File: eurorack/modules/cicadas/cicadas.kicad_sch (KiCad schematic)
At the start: 54 parts, among them J1 Conn_02x05_Odd_Even, J10 AudioJack2_SwitchT, J11 AudioJack2_SwitchT, J2 AVR-ISP-6, J3 AudioJack2_SwitchT, J4 AudioJack2_SwitchT, J5 AudioJack2_SwitchT, J6 AudioJack2_SwitchT, J7 AudioJack2_SwitchT, J8 AudioJack2_SwitchT, J9 AudioJack2_SwitchT, U1 L78L33_SOT89, U2 ATmega328P-A, U3 MCP4822, U4 MCP4822

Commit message: initial work on cicadas v3
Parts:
- removed C2: 100n, Capacitor_SMD:C_0805_2012Metric_Pad1.18x1.45mm_HandSolder, symbol Device:C
- removed D4: LED, LED_SMD:LED_0805_2012Metric_Pad1.15x1.40mm_HandSolder, symbol Device:LED
- removed J2: AVR-ISP-6, Connector_PinHeader_2.54mm:PinHeader_2x03_P2.54mm_Vertical_SMD, symbol Connector:AVR-ISP-6
- removed R2: R, Resistor_SMD:R_0805_2012Metric_Pad1.20x1.40mm_HandSolder, symbol Device:R
- removed TP1: 3.3V, TestPoint:TestPoint_Pad_D1.5mm, symbol Connector:TestPoint
- removed TP10: B, TestPoint:TestPoint_Pad_D1.5mm, symbol Connector:TestPoint
- removed TP11: A4, TestPoint:TestPoint_Pad_D1.5mm, symbol Connector:TestPoint
- removed TP12: A3, TestPoint:TestPoint_Pad_D1.5mm, symbol Connector:TestPoint
- removed TP13: GND, TestPoint:TestPoint_Pad_D1.5mm, symbol Connector:TestPoint
- removed TP2: D4, TestPoint:TestPoint_Pad_D1.5mm, symbol Connector:TestPoint
- removed TP3: D3, TestPoint:TestPoint_Pad_D1.5mm, symbol Connector:TestPoint
- removed TP4: D2, TestPoint:TestPoint_Pad_D1.5mm, symbol Connector:TestPoint
- removed TP5: A2, TestPoint:TestPoint_Pad_D1.5mm, symbol Connector:TestPoint
- removed TP6: D1, TestPoint:TestPoint_Pad_D1.5mm, symbol Connector:TestPoint
- removed TP7: A1, TestPoint:TestPoint_Pad_D1.5mm, symbol Connector:TestPoint
- removed TP8: R, TestPoint:TestPoint_Pad_D1.5mm, symbol Connector:TestPoint
- removed TP9: G, TestPoint:TestPoint_Pad_D1.5mm, symbol Connector:TestPoint
- removed U1: L78L33_SOT89, Package_TO_SOT_SMD:SOT-89-3, symbol Regulator_Linear:L78L33_SOT89
- removed U2: ATmega328P-A, Package_QFP:TQFP-32_7x7mm_P0.8mm, symbol MCU_Microchip_ATmega:ATmega328P-A
- added D10, D11, D4, D5, D6, D7, D8, D9: SK6812MINI, Pale Slim Ghost:SK6812MINI-E, symbol kbd:YS-SK6812MINI-E
- added G1, G2: (no value), symbol Pale Slim Ghost:Artwork
- added H1, H10, H11, H12, H2, H3, H4, H5, H6, H7, H8, H9: (no value), symbol Mechanical:MountingHole
- added U1: ProMicro, promicro:ProMicro-NoSilk, symbol promicro:ProMicro
- J10, J11, J3, J4, J5, J6, J7, J8, J9: footprint AudioJacks:Jack_3.5mm_QingPu_WQP-PJ398SM_Vertical -> (none)
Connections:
- net +12V: now also U1.24 (RAW)
- net +3V3: now also D10.1 (VDD), D11.1 (VDD), D4.1 (VDD), D5.1 (VDD), D6.1 (VDD), D7.1 (VDD), D8.1 (VDD), D9.1 (VDD), U1.21 (VCC)
- net CIPO: now also U1.15 (B3)
- net COPI: now also U1.14 (B2)
- net CS1: now also U1.12 (B5)
- net CS2: now also U1.11 (B4)
- net D1: now also U1.17 (F7)
- net D2: now also U1.18 (F6)
- net D3: now also U1.19 (F5)
- net D4: now also U1.20 (F4)
- net GND: now also D10.3 (VSS), D11.3 (VSS), D4.3 (VSS), D5.3 (VSS), D6.3 (VSS), D7.3 (VSS), D8.3 (VSS), D9.3 (VSS), U1.23 (GND), U1.3 (GND), U1.4 (GND)
- net LED B: now also U1.9 (D7)
- net LED G: now also U1.8 (C6)
- net LED R: now also U1.6 (SCL)
- net SCK: now also U1.16 (B1)
- net clock in: now also U1.5 (SDA)
- net encoder A: now also U1.1 (TX)
- net encoder B: now also U1.2 (RX)
- net switch: now also U1.7 (D4)
- new net: D10.4 (DIN), D9.2 (DOUT)
- new net: D8.2 (DOUT), D9.4 (DIN)
- new net: D7.2 (DOUT), D8.4 (DIN)
- new net: D6.2 (DOUT), D7.4 (DIN)
- new net: D10.2 (DOUT), D11.4 (DIN)
- new net: D4.2 (DOUT), D5.4 (DIN)
- new net: D5.2 (DOUT), D6.4 (DIN)
- new net LED: D4.4 (DIN), U1.13 (B6)
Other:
- moved on the sheet: C1, C4, D1, D2, J1

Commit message: cicadas footprint associations
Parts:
- G1: value (none) -> Artwork; footprint (none) -> Pale Slim Ghost:logo
- G2: value (none) -> Artwork
- H1, H12: value (none) -> MountingHole; footprint (none) -> Pale Slim Ghost:eurorack panel mounting slot
- H10, H11, H2, H4, H5, H6, H7, H8, H9: value (none) -> MountingHole; footprint (none) -> Pale Slim Ghost:hole 6mm (jack panel)
- H3: value (none) -> MountingHole; footprint (none) -> Pale Slim Ghost:hole 9mm (encoder panel)
- J10, J11, J3, J4, J5, J6, J7, J8, J9: footprint (none) -> Pale Slim Ghost:Jack_3.5mm_QingPu_WQP-PJ398SM_Vertical

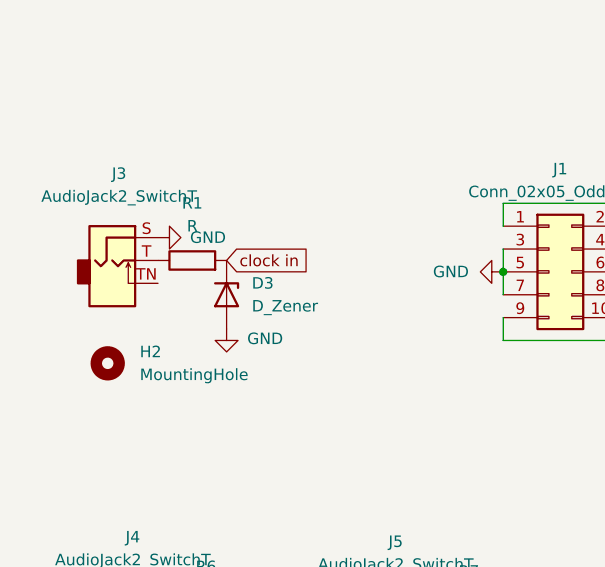
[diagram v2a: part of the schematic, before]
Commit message: cicadas: normal clock input to 3v3 and fix missing ground connections
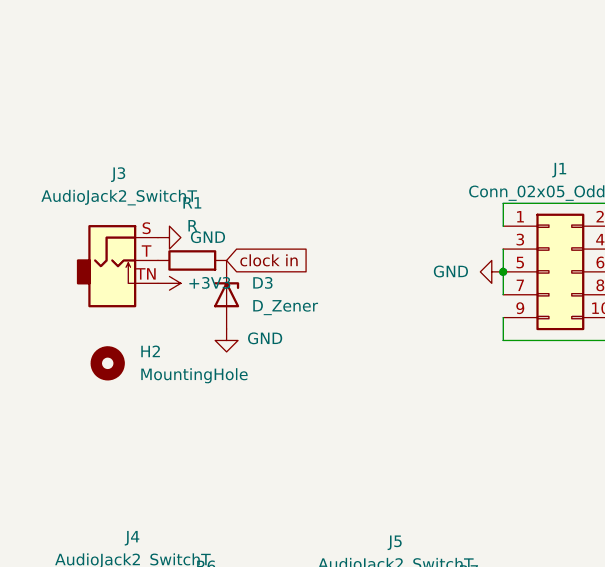
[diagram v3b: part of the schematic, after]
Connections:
- net +3V3: now also J3.TN
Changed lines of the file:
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@@
     (pin "9")
+  )
+  (symbol (lib_id "power:+3V3") (at 35.306 53.34 270) (unit 1)
+    (in_bom yes) (on_board yes) (fields_autoplaced)
+    (property "Reference" "#PWR?" (id 0) (at 31.496 53.34 0)
+      (effects (font (size 1.27 1.27)) hide)
+    )
+    (property "Value" "+3V3" (id 1) (at 38.608 53.3399 90)
+      (effects (font (size 1.27 1.27)) (justify left))
+    )
+    (property "Footprint" "" (id 2) (at 35.306 53.34 0)
+      (effects (font (size 1.27 1.27)) hide)
+    )
+    (property "Datasheet" "" (id 3) (at 35.306 53.34 0)
+      (effects (font (size 1.27 1.27)) hide)
+    )
+    (pin "1")
   )
   (symbol (lib_id "power:GND") (at 73.66 52.07 270) (unit 1)
@@
       (reference "#PWR0106") (unit 1) (value "GND") (footprint "")
     )
+    (path "/89197813-1f34-412e-b0f2-543175929a5d"
+      (reference "#PWR?") (unit 1) (value "+3V3") (footprint "")
+    )
     (path "/f39590a6-380e-454f-af5a-71361c77cf95"

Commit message: wip cicadas redesign
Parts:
- removed C1: 10u, Capacitor_SMD:CP_Elec_5x4.5, symbol Device:C_Polarized
- removed C4: 100n, Capacitor_SMD:C_0805_2012Metric_Pad1.18x1.45mm_HandSolder, symbol Device:C
- removed D1, D2: D, Diode_SMD:D_SOD-123, symbol Device:D
- removed G1: Artwork, Pale Slim Ghost:logo, symbol Pale Slim Ghost:Artwork
- removed G2: Artwork, symbol Pale Slim Ghost:Artwork
- removed J1: Conn_02x05_Odd_Even, Connector_PinHeader_2.54mm:PinHeader_2x05_P2.54mm_Vertical_SMD, symbol Connector_Generic:Conn_02x05_Odd_Even
- removed U1: ProMicro, promicro:ProMicro-NoSilk, symbol promicro:ProMicro
- added B1, B2: Mousebite, Pale Slim Ghost:mousebite-2.54x5.08mm, symbol Pale Slim Ghost:Mousebite
- added C1, C2: 10u, Capacitor_SMD:C_0805_2012Metric_Pad1.18x1.45mm_HandSolder, symbol Device:C
- added U1: MIC5219-5.0YM5, Package_TO_SOT_SMD:SOT-23-5, symbol Regulator_Linear:MIC5219-5.0YM5
- added U2: Chordata, Pale Slim Ghost:Chordata, symbol Pale Slim Ghost:Chordata
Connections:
- net +12V: now also C1.1, U1.1 (IN), U1.3 (EN), U2.17 (+12V)
- net +3V3: now also U2.36 (+3V3); no longer C6.1, C7.1, D10.1 (VDD), D11.1 (VDD), D4.1 (VDD), D5.1 (VDD), D6.1 (VDD), D7.1 (VDD), D8.1 (VDD), D9.1 (VDD), U3.1 (Vdd), U4.1 (Vdd)
- net COPI: now also U2.24 (GPIO19)
- net CS1: now also U2.22 (GPIO17)
- net CS2: now also U2.21 (GPIO16)
- net D1: now also U2.13 (GPIO12)
- net D2: now also U2.14 (GPIO13)
- net D3: now also U2.15 (GPIO14)
- net D4: now also U2.16 (GPIO15)
- net GND: now also C1.2, C2.2, U1.2 (GND), U2.18 (GND), U2.19 (GND), U2.35 (GND)
- net LED: now also U2.25 (GPIO20)
- net LED B: now also U2.7 (GPIO6)
- net LED G: now also U2.9 (GPIO8)
- net LED R: now also U2.10 (GPIO9)
- net SCK: now also U2.27 (GPIO22)
- net clock in: now also U2.1 (GPIO0)
- net encoder A: now also U2.12 (GPIO11)
- net encoder B: now also U2.11 (GPIO10)
- net switch: now also U2.8 (GPIO7)
- new net +5V: C2.1, C6.1, C7.1, D10.1 (VDD), D11.1 (VDD), D4.1 (VDD), D5.1 (VDD), D6.1 (VDD), D7.1 (VDD), D8.1 (VDD), D9.1 (VDD), U1.5 (OUT), U3.1 (Vdd), U4.1 (Vdd)
- no-connect marks 0 -> 1
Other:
- moved on the sheet: U4

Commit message: assorted changes ig from opening things in kicad 7
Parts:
- removed D10, D11, D4, D5, D6, D7, D8, D9: SK6812MINI, Pale Slim Ghost:SK6812MINI-E, symbol kbd:YS-SK6812MINI-E
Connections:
- net LED: no longer names the net of U2.25 (GPIO20)
